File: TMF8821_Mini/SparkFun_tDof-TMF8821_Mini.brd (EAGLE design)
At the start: 25.4 x 12.7 mm, 50 parts, among them J4 QWIIC_RIGHT_ANGLE, J5 QWIIC_RIGHT_ANGLE

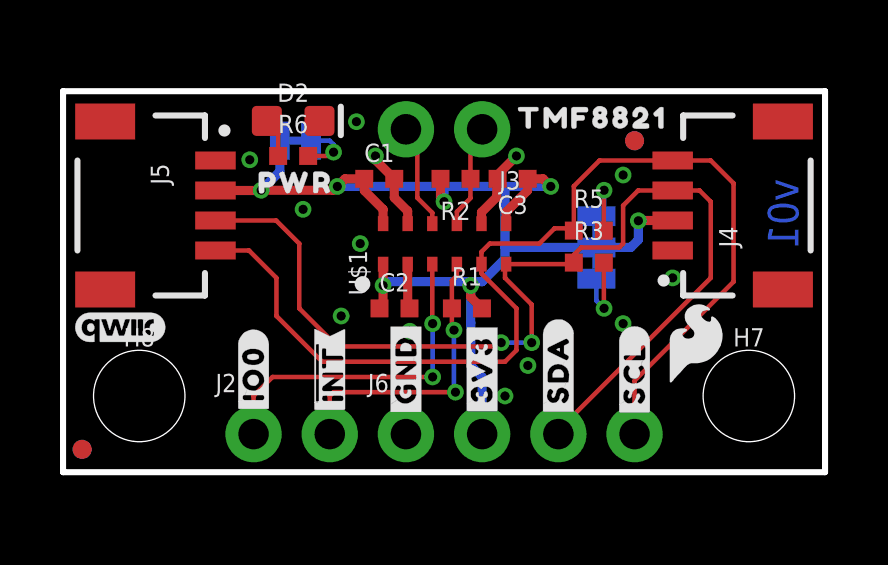
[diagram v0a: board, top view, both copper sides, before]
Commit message: Removes old production files
* Removes old 8821 "HQ" variants
* Copies the 8820 and 8820 Mini variants
* Adjusts new 8820 copies to reference 8821 and replaces 8820 with 8821
* Updates Product Identifier jumpers to reflect changes
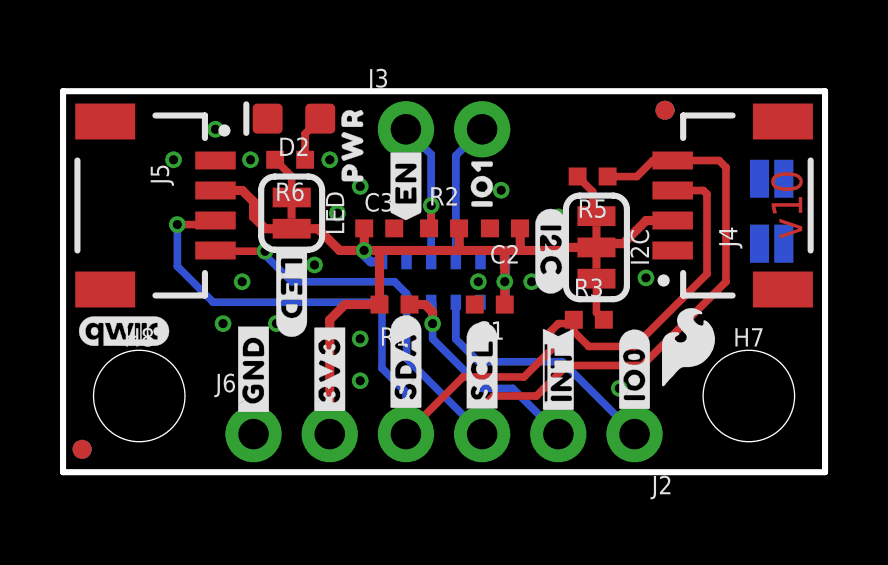
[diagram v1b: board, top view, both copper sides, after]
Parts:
- removed U$34: (no value), SparkFun-Aesthetics:OSHW-LOGO-MINI
- added TMF8820: JUMPER-SMT_2_NO_SILK, SparkFun-Jumpers:SMT-JUMPER_2_NO_SILK
- added TMF8821: JUMPER-SMT_2_NC_PASTE_SILK, SparkFun-Jumpers:SMT-JUMPER_2_NC_PASTE_SILK
- added U$11: (no value), TMFHQTopSilk:TMF882188210
- added U$12: (no value), TMFMiniTop:IO18
- LOGO1: value SFE_LOGO_NAME_FLAMEBLANK -> SFE_LOGO_NAMEBLANK
- U$8: device TMFHQTopSilk:TMF882188210 -> TMFMiniTop:TMF882020
- U$9: device TMFHQBotSilk:TMF882113 -> TMFHQTopSilk:#EN#7
- moved U$33 21.4 mm to (2.16, 8.76)
- moved U$7 14.0 mm to (18.9, 11.2)
- moved U$8 13.9 mm to (18.8, 9.65)
- moved U$5 12.7 mm to (19.1, 3.94)
- moved J2 12.7 mm to (19.1, 1.27), turned to 180 degrees
- moved U$2 12.7 mm to (19.1, 3.30)
- moved U$3 7.62 mm to (16.5, 3.30)
- moved U$4 7.62 mm to (16.5, 3.30)
- moved U$9 6.59 mm to (11.4, 9.65), turned to 90 degrees
- moved U$22 5.62 mm to (7.62, 6.10), flipped to the top, turned to 270 degrees
- moved C1 5.58 mm to (14.2, 5.59), turned to 180 degrees
- moved U$18 5.08 mm to (11.4, 3.56)
- moved U$40 5.08 mm to (11.4, 3.56)
- moved U$19 5.08 mm to (14.0, 3.43)
- moved U$39 5.08 mm to (14.0, 3.43)
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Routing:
- net 3.3V: track 40.7 -> 30.5 mm, vias 7 -> 2
- net GND: track 6.61 -> 0.00 mm, vias 13 -> 18
- net SCL: track 36.9 -> 31.6 mm, vias 0 -> 1
- net SDA: track 35.3 -> 32.1 mm, vias 2 -> 1
- net GPIO0/SYNC: track 11.3 -> 8.50 mm, vias 2 -> 0
- net EN: track 3.49 -> 5.56 mm, vias 0 -> 1
- net !INT!: track 9.90 -> 8.00 mm, vias 2 -> 1
- net GPIO1: track 3.51 -> 4.78 mm
- net N$7: track 2.62 -> 1.47 mm, vias 1 -> 0
- net N$8: track 2.32 -> 1.58 mm, vias 1 -> 0
- net N$6: track 1.95 -> 1.49 mm, vias 1 -> 0
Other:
- board text added: "v10"
- board text removed: "v01"

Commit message: Adds new product identifier pads to all designs, rolls 8820 version number to v10
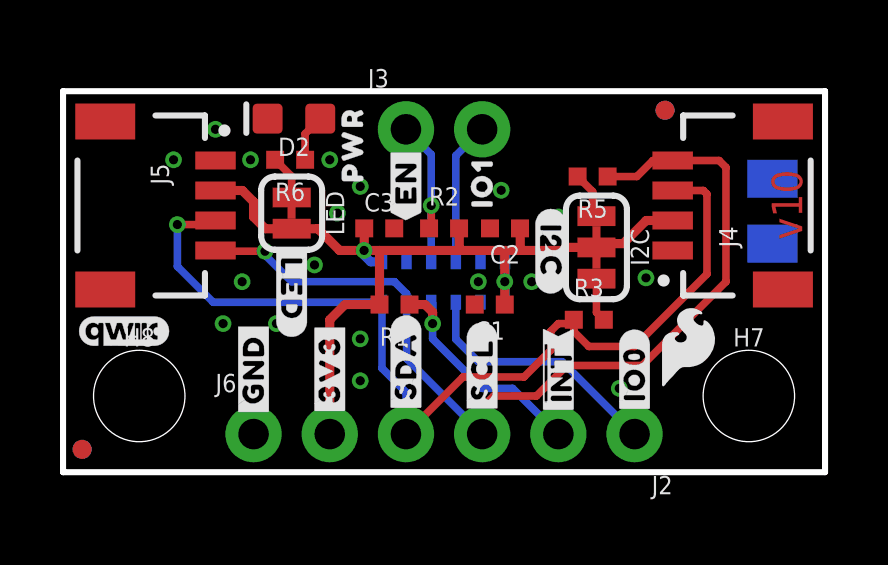
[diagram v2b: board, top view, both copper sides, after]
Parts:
- TMF8820: value JUMPER-SMT_2_NO_SILK -> PROD_ID_NO-PASTE_SILK; device SparkFun-Jumpers:SMT-JUMPER_2_NO_SILK -> SparkFun-Aesthetics:PRODUCT_IDENT_NO_SILK
- TMF8821: value JUMPER-SMT_2_NC_PASTE_SILK -> PROD_ID_PASTE_SILK; device SparkFun-Jumpers:SMT-JUMPER_2_NC_PASTE_SILK -> SparkFun-Aesthetics:PRODUCT_IDENT_PASTE_SILK
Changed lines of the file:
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@@
 <drawing>
 <settings>
-<setting alwaysvectorfont="yes"/>
+<setting alwaysvectorfont="no"/>
 <setting verticaltext="up"/>
 </settings>
@@
 <layer number="30" name="bStop" color="7" fill="6" visible="no" active="yes"/>
 <layer number="31" name="tCream" color="7" fill="4" visible="no" active="yes"/>
-<layer number="32" name="bCream" color="7" fill="5" visible="yes" active="yes"/>
+<layer number="32" name="bCream" color="7" fill="5" visible="no" active="yes"/>
 <layer number="33" name="tFinish" color="6" fill="3" visible="no" active="yes"/>
 <layer number="34" name="bFinish" color="6" fill="6" visible="no" active="yes"/>
@@
 <layer number="115" name="ReferenceISLANDS" color="7" fill="1" visible="no" active="no"/>
 <layer number="116" name="Patch_BOT" color="9" fill="4" visible="no" active="no"/>
-<layer number="117" name="PM_Ref" color="26" fill="1" visible="no" active="yes"/>
+<layer number="117" name="PM_Ref" color="26" fill="1" visible="yes" active="yes"/>
 <layer number="118" name="Rect_Pads" color="7" fill="1" visible="no" active="no"/>
-<layer number="119" name="PF_Ref" color="31" fill="1" visible="no" active="yes"/>
-<layer number="120" name="WFL_Ref" color="25" fill="1" visible="no" active="yes"/>
+<layer number="119" name="PF_Ref" color="31" fill="1" visible="yes" active="yes"/>
+<layer number="120" name="WFL_Ref" color="25" fill="1" visible="yes" active="yes"/>
 <layer number="121" name="_tsilk" color="7" fill="1" visible="no" active="no"/>
 <layer number="122" name="_bsilk" color="7" fill="1" visible="no" active="no"/>
@@
 <element name="LOGO3" library="SparkFun-Aesthetics" package="DUMMY" value="OSHW-LOGONO_SILK" x="-11.938" y="-12.954" smashed="yes"/>
 <element name="U$2" library="TMFHQTopSilk" package="#IO0#8" value="" x="19.05" y="3.302" smashed="yes" rot="R90"/>
-<element name="TMF8820" library="SparkFun-Jumpers" package="SMT-JUMPER_2_NO_SILK" package3d_urn="urn:adsk.eagle:package:39279/1" value="JUMPER-SMT_2_NO_SILK" x="23.622" y="9.779" smashed="yes" rot="MR0">
+<element name="TMF8820" library="SparkFun-Aesthetics" package="PRODUCT_IDENT_NO_SILK" value="PROD_ID_NO-PASTE_SILK" x="23.622" y="9.779" smashed="yes" rot="MR0">
 <attribute name="NAME" x="23.622" y="10.922" size="0.6096" layer="26" font="vector" ratio="20" rot="MR0" align="bottom-center"/>
 <attribute name="VALUE" x="23.622" y="8.636" size="0.6096" layer="28" font="vector" ratio="20" rot="MR0" align="top-center"/>
 </element>
-<element name="TMF8821" library="SparkFun-Jumpers" package="SMT-JUMPER_2_NC_PASTE_SILK" package3d_urn="urn:adsk.eagle:package:39282/1" value="JUMPER-SMT_2_NC_PASTE_SILK" x="23.622" y="7.62" smashed="yes" rot="MR0">
+<element name="TMF8821" library="SparkFun-Aesthetics" package="PRODUCT_IDENT_PASTE_SILK" value="PROD_ID_PASTE_SILK" x="23.622" y="7.62" smashed="yes" rot="MR0">
 <attribute name="NAME" x="23.622" y="8.763" size="0.6096" layer="26" font="vector" ratio="20" rot="MR0" align="bottom-center"/>
 <attribute name="VALUE" x="23.622" y="6.477" size="0.6096" layer="28" font="vector" ratio="20" rot="MR0" align="top-center"/>

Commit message: Changes all "IO" silk to be "GP" instead, increases Qwiic pill size on mini's
* Fixes orientation of I2C and LED silk on mini versions
* Increases SparkFun flame size on mini versions
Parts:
- removed U$22: (no value), TMFHQBotSilk:#LED#10
- removed U$33: (no value), SparkFun-Aesthetics:SFE_LOGO_FLAME_.1
- added U$13: (no value), TMFMiniTop:#GP0#19
- added U$14: (no value), SparkFun-Aesthetics:SFE_LOGO_FLAME_.2
- LOGO2: value QWIIC_LOGO_3MM -> QWIIC_LOGO_4MM; device SparkFun-Aesthetics:QWIIC_3MM -> SparkFun-Aesthetics:QWIIC_4MM
- U$12: device TMFMiniTop:IO18 -> TMFMiniTop:GP18
- U$2: device TMFHQTopSilk:#IO0#8 -> TMFMiniBotSilk:#LED#10
- U$6: device TMFHQTopSilk:#IO1#8 -> TMFMiniBotSilk:#GP1#8
- moved U$2 11.6 mm to (7.75, 6.10)
- moved U$20 0.25 mm to (16.3, 7.62), turned to 90 degrees
- moved U$6 0.13 mm to (14.0, 9.40)
- moved LOGO2 0.13 mm to (2.16, 4.70)
- moved U$12 0.13 mm to (14.0, 9.53)
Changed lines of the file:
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@@
 <drawing>
 <settings>
-<setting alwaysvectorfont="no"/>
+<setting alwaysvectorfont="yes"/>
 <setting verticaltext="up"/>
 </settings>
@@
 <element name="U$18" library="TMFHQBotSilk" package="#SDA#6" value="" x="11.43" y="3.556" smashed="yes" rot="MR270"/>
 <element name="U$19" library="TMFHQBotSilk" package="#SCL#5" value="" x="13.97" y="3.429" smashed="yes" rot="MR270"/>
-<element name="U$20" library="TMFHQBotSilk" package="#I2C#11" value="" x="16.256" y="7.366" smashed="yes" rot="R270"/>
-<element name="U$22" library="TMFHQBotSilk" package="#LED#10" value="" x="7.62" y="6.096" smashed="yes" rot="R270"/>
-<element name="U$33" library="SparkFun-Aesthetics" package="SFE_LOGO_FLAME_.1" value="" x="2.159" y="8.763" smashed="yes" rot="MR0"/>
+<element name="U$20" library="TMFHQBotSilk" package="#I2C#11" value="" x="16.256" y="7.62" smashed="yes" rot="R90"/>
 <element name="U$35" library="SparkFun-Aesthetics" package="SFE_LOGO_FLAME_.1" value="" x="20.828" y="4.191" smashed="yes"/>
 <element name="U$37" library="TMFHQTopSilk" package="#3V3#0" value="" x="8.89" y="3.429" smashed="yes" rot="R90"/>
@@
 <element name="U$4" library="TMFHQTopSilk" package="##INT##8" value="" x="16.51" y="3.302" smashed="yes" rot="MR270"/>
 <element name="U$5" library="TMFHQBotSilk" package="#SYNC#8" value="" x="19.05" y="3.937" smashed="yes" rot="MR270"/>
-<element name="U$6" library="TMFHQTopSilk" package="#IO1#8" value="" x="13.97" y="9.525" smashed="yes" rot="MR270"/>
 <element name="U$7" library="TMFHQTopSilk" package="DTOF882188211" value="" x="18.923" y="11.176" smashed="yes" rot="MR0"/>
 <element name="LOGO1" library="SparkFun-Aesthetics" package="BLANK" value="SFE_LOGO_NAMEBLANK" x="-11.938" y="-12.954" smashed="yes"/>
-<element name="LOGO2" library="SparkFun-Aesthetics" package="QWIIC_3MM" value="QWIIC_LOGO_3MM" x="2.032" y="4.699" smashed="yes"/>
 <element name="LOGO3" library="SparkFun-Aesthetics" package="DUMMY" value="OSHW-LOGONO_SILK" x="-11.938" y="-12.954" smashed="yes"/>
-<element name="U$2" library="TMFHQTopSilk" package="#IO0#8" value="" x="19.05" y="3.302" smashed="yes" rot="R90"/>
 <element name="TMF8820" library="SparkFun-Aesthetics" package="PRODUCT_IDENT_NO_SILK" value="PROD_ID_NO-PASTE_SILK" x="23.622" y="9.779" smashed="yes" rot="MR0">
 <attribute name="NAME" x="23.622" y="10.922" size="0.6096" layer="26" font="vector" ratio="20" rot="MR0" align="bottom-center"/>
@@
 <element name="U$9" library="TMFHQTopSilk" package="#EN#7" value="" x="11.43" y="9.652" smashed="yes" rot="R90"/>
 <element name="U$11" library="TMFHQTopSilk" package="TMF882188210" value="" x="18.923" y="7.62" smashed="yes" rot="MR0"/>
-<element name="U$12" library="TMFMiniTop" package="IO18" value="" x="13.97" y="9.652" smashed="yes" rot="R90"/>
 <element name="U$8" library="TMFMiniTop" package="TMF882020" value="" x="18.796" y="9.652" smashed="yes" rot="MR0"/>
+<element name="LOGO2" library="SparkFun-Aesthetics" package="QWIIC_4MM" value="QWIIC_LOGO_4MM" x="2.159" y="4.699" smashed="yes"/>
+<element name="U$2" library="TMFMiniBotSilk" package="#LED#10" value="" x="7.747" y="6.096" smashed="yes" rot="R90"/>
+<element name="U$6" library="TMFMiniBotSilk" package="#GP1#8" value="" x="13.97" y="9.398" smashed="yes" rot="MR270"/>
+<element name="U$12" library="TMFMiniTop" package="GP18" value="" x="13.97" y="9.525" smashed="yes" rot="R90"/>
+<element name="U$13" library="TMFMiniTop" package="#GP0#19" value="" x="19.05" y="3.429" smashed="yes" rot="R90"/>
+<element name="U$14" library="SparkFun-Aesthetics" package="SFE_LOGO_FLAME_.2" value="" x="2.54" y="8.89" smashed="yes" rot="MR0"/>
 </elements>
 <signals>

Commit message: Adds OSHW logo to boards, fixes silk width of new product identifier pads
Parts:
- added U$15: (no value), SparkFun-Aesthetics:OSHW-LOGO-MINI
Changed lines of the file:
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@@
 <drawing>
 <settings>
-<setting alwaysvectorfont="yes"/>
+<setting alwaysvectorfont="no"/>
 <setting verticaltext="up"/>
 </settings>
@@
 <element name="U$13" library="TMFMiniTop" package="#GP0#19" value="" x="19.05" y="3.429" smashed="yes" rot="R90"/>
 <element name="U$14" library="SparkFun-Aesthetics" package="SFE_LOGO_FLAME_.2" value="" x="2.54" y="8.89" smashed="yes" rot="MR0"/>
+<element name="U$15" library="SparkFun-Aesthetics" package="OSHW-LOGO-MINI" value="" x="2.54" y="5.715" smashed="yes" rot="MR0"/>
 </elements>
 <signals>
